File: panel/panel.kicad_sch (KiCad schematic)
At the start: 32 parts

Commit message: Moving panel to subfolder
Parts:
- J? (x2): footprint ledcube:5034800600 -> panel:5034800600
- U? (x2): symbol ledcube:SN74HC595 -> panel:SN74HC595
- U? (x3): symbol ledcube:TLC59025 -> panel:TLC59025
- U? (x2): symbol ledcube:NC7WZ17 -> panel:NC7WZ17

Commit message: Annotated schematic
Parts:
- gave numbers to parts that had none: 32

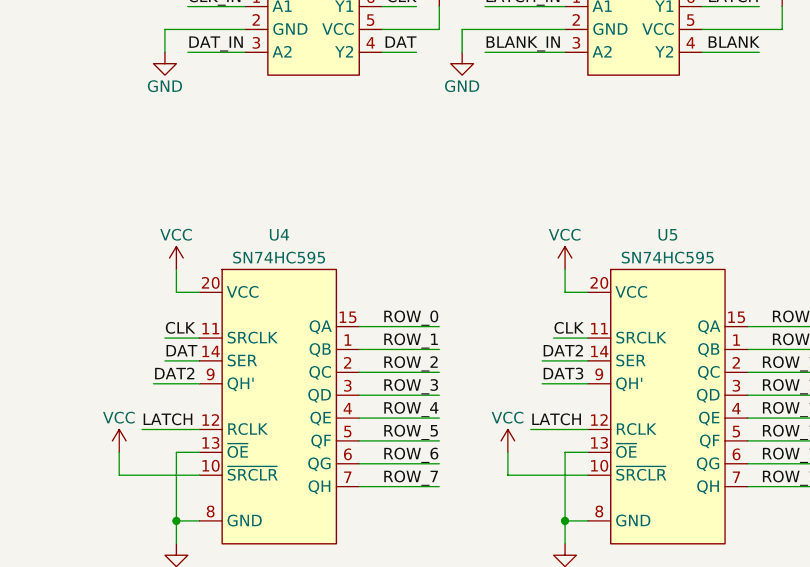
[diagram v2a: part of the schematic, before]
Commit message: LED matrix placement
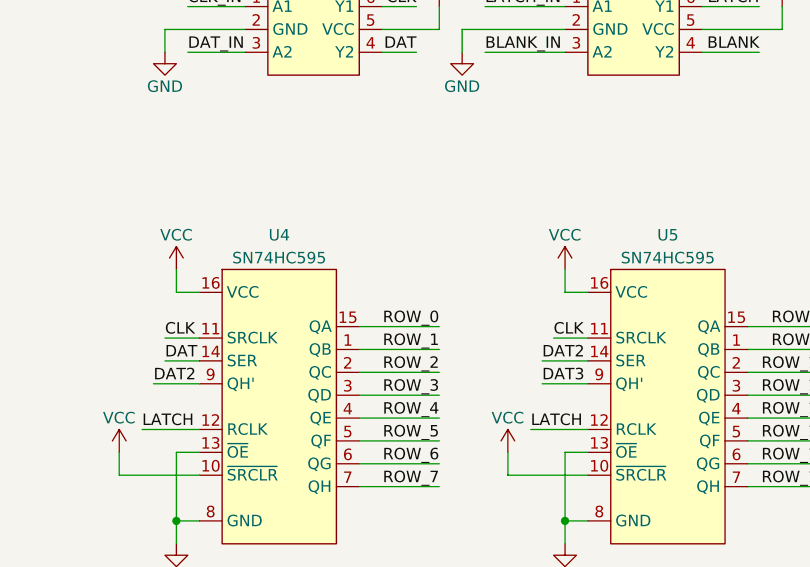
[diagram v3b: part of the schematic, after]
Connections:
- net VCC: now also U4.16 (VCC), U5.16 (VCC); no longer U4.20 (VCC), U5.20 (VCC)
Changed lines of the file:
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@@
     (pin "14")
     (pin "15")
+    (pin "16")
     (pin "2")
-    (pin "20")
     (pin "3")
     (pin "4")
@@
     (pin "14")
     (pin "15")
+    (pin "16")
     (pin "2")
-    (pin "20")
     (pin "3")
     (pin "4")
@@
     (pin "9")
   )
-  (symbol (lib_id "panel:TLC59025") (at 46.99 142.24 0) (unit 1)
+  (symbol (lib_name "panel:TLC59025_1") (lib_id "panel:TLC59025") (at 46.99 142.24 0) (unit 1)
     (in_bom yes) (on_board yes) (fields_autoplaced)
     (property "Reference" "U1" (id 0) (at 46.99 138.43 0))
@@
     (pin "9")
   )
-  (symbol (lib_id "panel:TLC59025") (at 90.17 142.24 0) (unit 1)
+  (symbol (lib_name "panel:TLC59025_2") (lib_id "panel:TLC59025") (at 90.17 142.24 0) (unit 1)
     (in_bom yes) (on_board yes) (fields_autoplaced)
     (property "Reference" "U2" (id 0) (at 90.17 138.43 0))

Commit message: Routed all data signals
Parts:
- Q1, Q10, Q11, Q12, Q13, Q14, Q15, Q16, Q2, Q3, Q4, Q5, Q6, Q7, Q8, Q9: footprint Package_TO_SOT_SMD:SOT-883 -> panel:SOT-883
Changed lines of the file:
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@@
       (effects (font (size 1.27 1.27)) (justify left) hide)
     )
-    (property "Footprint" "Package_TO_SOT_SMD:SOT-883" (id 2) (at 203.2 48.26 0)
+    (property "Footprint" "panel:SOT-883" (id 2) (at 203.2 48.26 0)
       (effects (font (size 1.27 1.27)) hide)
     )
@@
       (effects (font (size 1.27 1.27)) (justify left) hide)
     )
-    (property "Footprint" "Package_TO_SOT_SMD:SOT-883" (id 2) (at 203.2 59.69 0)
+    (property "Footprint" "panel:SOT-883" (id 2) (at 203.2 59.69 0)
       (effects (font (size 1.27 1.27)) hide)
     )
@@
       (effects (font (size 1.27 1.27)) (justify left) hide)
     )
-    (property "Footprint" "Package_TO_SOT_SMD:SOT-883" (id 2) (at 203.2 71.12 0)
+    (property "Footprint" "panel:SOT-883" (id 2) (at 203.2 71.12 0)
       (effects (font (size 1.27 1.27)) hide)
     )
@@
       (effects (font (size 1.27 1.27)) (justify left) hide)
     )
-    (property "Footprint" "Package_TO_SOT_SMD:SOT-883" (id 2) (at 203.2 82.55 0)
+    (property "Footprint" "panel:SOT-883" (id 2) (at 203.2 82.55 0)
       (effects (font (size 1.27 1.27)) hide)
     )
@@
       (effects (font (size 1.27 1.27)) (justify left) hide)
     )
-    (property "Footprint" "Package_TO_SOT_SMD:SOT-883" (id 2) (at 203.2 93.98 0)
+    (property "Footprint" "panel:SOT-883" (id 2) (at 203.2 93.98 0)
       (effects (font (size 1.27 1.27)) hide)
     )
@@
       (effects (font (size 1.27 1.27)) (justify left) hide)
     )
-    (property "Footprint" "Package_TO_SOT_SMD:SOT-883" (id 2) (at 203.2 105.41 0)
+    (property "Footprint" "panel:SOT-883" (id 2) (at 203.2 105.41 0)
       (effects (font (size 1.27 1.27)) hide)
     )
@@
       (effects (font (size 1.27 1.27)) (justify left) hide)
     )
-    (property "Footprint" "Package_TO_SOT_SMD:SOT-883" (id 2) (at 203.2 116.84 0)
+    (property "Footprint" "panel:SOT-883" (id 2) (at 203.2 116.84 0)
       (effects (font (size 1.27 1.27)) hide)
     )
@@
       (effects (font (size 1.27 1.27)) (justify left) hide)
     )
-    (property "Footprint" "Package_TO_SOT_SMD:SOT-883" (id 2) (at 203.2 128.27 0)
+    (property "Footprint" "panel:SOT-883" (id 2) (at 203.2 128.27 0)
       (effects (font (size 1.27 1.27)) hide)
     )
@@
       (effects (font (size 1.27 1.27)) (justify left) hide)
     )
-    (property "Footprint" "Package_TO_SOT_SMD:SOT-883" (id 2) (at 250.19 48.26 0)
+    (property "Footprint" "panel:SOT-883" (id 2) (at 250.19 48.26 0)
       (effects (font (size 1.27 1.27)) hide)
     )
@@
       (effects (font (size 1.27 1.27)) (justify left) hide)
     )
-    (property "Footprint" "Package_TO_SOT_SMD:SOT-883" (id 2) (at 250.19 59.69 0)
+    (property "Footprint" "panel:SOT-883" (id 2) (at 250.19 59.69 0)
       (effects (font (size 1.27 1.27)) hide)
     )
@@
       (effects (font (size 1.27 1.27)) (justify left) hide)
     )
-    (property "Footprint" "Package_TO_SOT_SMD:SOT-883" (id 2) (at 250.19 71.12 0)
+    (property "Footprint" "panel:SOT-883" (id 2) (at 250.19 71.12 0)
       (effects (font (size 1.27 1.27)) hide)
     )
@@
       (effects (font (size 1.27 1.27)) (justify left) hide)
     )
-    (property "Footprint" "Package_TO_SOT_SMD:SOT-883" (id 2) (at 250.19 82.55 0)
+    (property "Footprint" "panel:SOT-883" (id 2) (at 250.19 82.55 0)
       (effects (font (size 1.27 1.27)) hide)
     )
@@
       (effects (font (size 1.27 1.27)) (justify left) hide)
     )
-    (property "Footprint" "Package_TO_SOT_SMD:SOT-883" (id 2) (at 250.19 93.98 0)
+    (property "Footprint" "panel:SOT-883" (id 2) (at 250.19 93.98 0)
       (effects (font (size 1.27 1.27)) hide)
     )
@@
       (effects (font (size 1.27 1.27)) (justify left) hide)
     )
-    (property "Footprint" "Package_TO_SOT_SMD:SOT-883" (id 2) (at 250.19 105.41 0)
+    (property "Footprint" "panel:SOT-883" (id 2) (at 250.19 105.41 0)
       (effects (font (size 1.27 1.27)) hide)
     )
@@
       (effects (font (size 1.27 1.27)) (justify left) hide)
     )
-    (property "Footprint" "Package_TO_SOT_SMD:SOT-883" (id 2) (at 250.19 116.84 0)
+    (property "Footprint" "panel:SOT-883" (id 2) (at 250.19 116.84 0)
       (effects (font (size 1.27 1.27)) hide)
     )
@@
       (effects (font (size 1.27 1.27)) (justify left) hide)
     )
-    (property "Footprint" "Package_TO_SOT_SMD:SOT-883" (id 2) (at 250.19 128.27 0)
+    (property "Footprint" "panel:SOT-883" (id 2) (at 250.19 128.27 0)
       (effects (font (size 1.27 1.27)) hide)
     )
@@
     )
     (path "/540dc0a0-cb0b-4dfb-87f6-511342a2796f"
-      (reference "Q1") (unit 1) (value "Q_PMOS_GSD") (footprint "Package_TO_SOT_SMD:SOT-883")
+      (reference "Q1") (unit 1) (value "Q_PMOS_GSD") (footprint "panel:SOT-883")
     )
     (path "/6df639de-66aa-4f8e-934a-38515961a4c1"
-      (reference "Q2") (unit 1) (value "Q_PMOS_GSD") (footprint "Package_TO_SOT_SMD:SOT-883")
+      (reference "Q2") (unit 1) (value "Q_PMOS_GSD") (footprint "panel:SOT-883")
     )
     (path "/1662c1e9-d071-4672-a50a-d59632799096"
-      (reference "Q3") (unit 1) (value "Q_PMOS_GSD") (footprint "Package_TO_SOT_SMD:SOT-883")
+      (reference "Q3") (unit 1) (value "Q_PMOS_GSD") (footprint "panel:SOT-883")
     )
     (path "/e62bc1a4-9007-492e-9214-cdaf7f9883a8"
-      (reference "Q4") (unit 1) (value "Q_PMOS_GSD") (footprint "Package_TO_SOT_SMD:SOT-883")
+      (reference "Q4") (unit 1) (value "Q_PMOS_GSD") (footprint "panel:SOT-883")
     )
     (path "/b0fe76a1-e7b8-4c55-ba03-bdfd4116e876"
-      (reference "Q5") (unit 1) (value "Q_PMOS_GSD") (footprint "Package_TO_SOT_SMD:SOT-883")
+      (reference "Q5") (unit 1) (value "Q_PMOS_GSD") (footprint "panel:SOT-883")
     )
     (path "/f9b833db-6f56-4fac-a5e4-cddc32cf4c6b"
-      (reference "Q6") (unit 1) (value "Q_PMOS_GSD") (footprint "Package_TO_SOT_SMD:SOT-883")
+      (reference "Q6") (unit 1) (value "Q_PMOS_GSD") (footprint "panel:SOT-883")
     )
     (path "/1979edeb-c786-4256-9b38-790a807c310d"
-      (reference "Q7") (unit 1) (value "Q_PMOS_GSD") (footprint "Package_TO_SOT_SMD:SOT-883")
+      (reference "Q7") (unit 1) (value "Q_PMOS_GSD") (footprint "panel:SOT-883")
     )
     (path "/7d404bbb-94fd-4b28-9150-5e5942e1a641"
-      (reference "Q8") (unit 1) (value "Q_PMOS_GSD") (footprint "Package_TO_SOT_SMD:SOT-883")
+      (reference "Q8") (unit 1) (value "Q_PMOS_GSD") (footprint "panel:SOT-883")
     )
     (path "/6f3a29fc-6cb3-44c9-948c-d864912cc61c"
-      (reference "Q9") (unit 1) (value "Q_PMOS_GSD") (footprint "Package_TO_SOT_SMD:SOT-883")
+      (reference "Q9") (unit 1) (value "Q_PMOS_GSD") (footprint "panel:SOT-883")
     )
     (path "/d31cec0c-c84b-4cf9-a596-e42b38fcb696"
-      (reference "Q10") (unit 1) (value "Q_PMOS_GSD") (footprint "Package_TO_SOT_SMD:SOT-883")
+      (reference "Q10") (unit 1) (value "Q_PMOS_GSD") (footprint "panel:SOT-883")
     )
     (path "/0a43e7b4-017b-4935-978c-84fb9a5a6cc0"
-      (reference "Q11") (unit 1) (value "Q_PMOS_GSD") (footprint "Package_TO_SOT_SMD:SOT-883")
+      (reference "Q11") (unit 1) (value "Q_PMOS_GSD") (footprint "panel:SOT-883")
     )
     (path "/5e86269f-d809-4ae3-ae14-44b60a3b5dec"
-      (reference "Q12") (unit 1) (value "Q_PMOS_GSD") (footprint "Package_TO_SOT_SMD:SOT-883")
+      (reference "Q12") (unit 1) (value "Q_PMOS_GSD") (footprint "panel:SOT-883")
     )
     (path "/1fdad119-9c7a-4284-83e9-942858cd8950"
-      (reference "Q13") (unit 1) (value "Q_PMOS_GSD") (footprint "Package_TO_SOT_SMD:SOT-883")
+      (reference "Q13") (unit 1) (value "Q_PMOS_GSD") (footprint "panel:SOT-883")
     )
     (path "/b6fd7422-90bb-4e64-886e-0887f176a800"
-      (reference "Q14") (unit 1) (value "Q_PMOS_GSD") (footprint "Package_TO_SOT_SMD:SOT-883")
+      (reference "Q14") (unit 1) (value "Q_PMOS_GSD") (footprint "panel:SOT-883")
     )
     (path "/77755fd0-ff8f-4a33-bd6a-dc738f7f8057"
-      (reference "Q15") (unit 1) (value "Q_PMOS_GSD") (footprint "Package_TO_SOT_SMD:SOT-883")
+      (reference "Q15") (unit 1) (value "Q_PMOS_GSD") (footprint "panel:SOT-883")
     )
     (path "/d1db849d-984c-4d78-a6a1-13bc0eace430"
-      (reference "Q16") (unit 1) (value "Q_PMOS_GSD") (footprint "Package_TO_SOT_SMD:SOT-883")
+      (reference "Q16") (unit 1) (value "Q_PMOS_GSD") (footprint "panel:SOT-883")
     )
     (path "/52b80c72-d096-46bf-b96a-1dc1d5e2cd56"

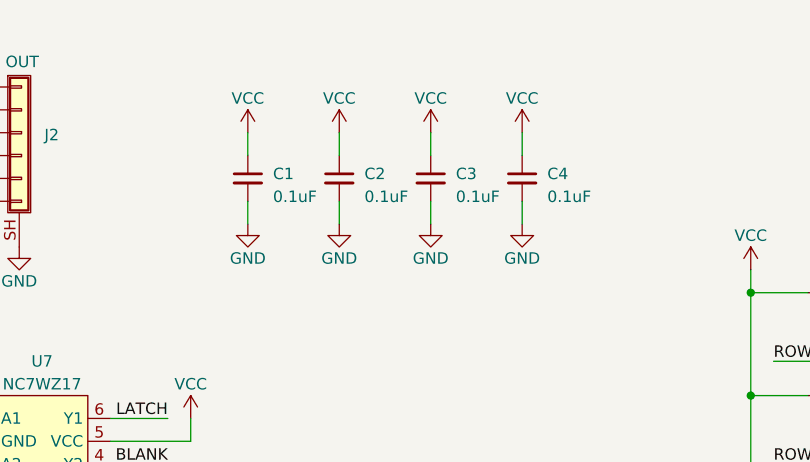
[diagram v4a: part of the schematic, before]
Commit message: Placed decoupling caps
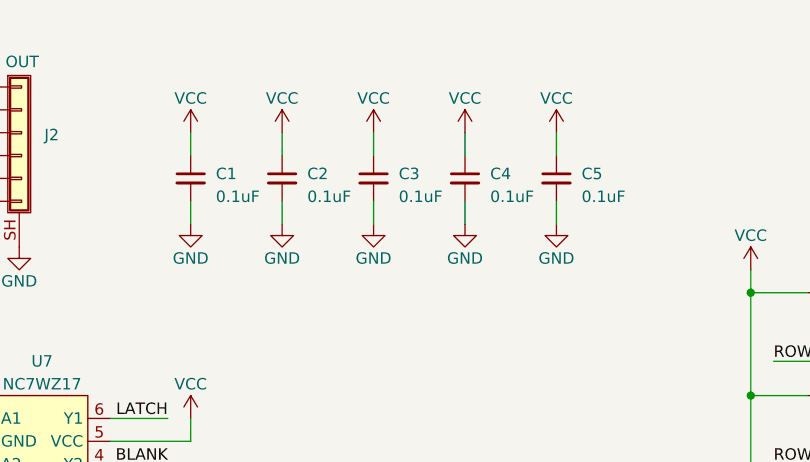
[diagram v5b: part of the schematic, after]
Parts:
- added C5: 0.1uF, Capacitor_SMD:C_0402_1005Metric, symbol Device:C_Small
- C1, C2, C3, C4: footprint Capacitor_SMD:C_0603_1608Metric -> Capacitor_SMD:C_0402_1005Metric
- R1, R2, R3: footprint Resistor_SMD:R_0603_1608Metric -> Resistor_SMD:R_0402_1005Metric
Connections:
- net GND: now also C5.2
- net VCC: now also C5.1
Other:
- moved on the sheet: C1, C2, C3, C4

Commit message: Silkscreen cleanup
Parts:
- C1, C2, C3, C4, C5: footprint Capacitor_SMD:C_0402_1005Metric -> panel:C_0402_1005Metric
- R1, R2, R3: footprint Resistor_SMD:R_0402_1005Metric -> panel:R_0402_1005Metric
- U1, U2, U3: footprint Package_SO:SSOP-24_3.9x8.7mm_P0.635mm -> panel:SSOP-24_3.9x8.7mm_P0.635mm
- U4, U5: footprint Package_SO:TSSOP-16_4.4x5mm_P0.65mm -> panel:TSSOP-16_4.4x5mm_P0.65mm
- U6, U7: footprint Package_SON:Fairchild_MicroPak2-6_1.0x1.0mm_P0.35mm -> panel:Fairchild_MicroPak2-6_1.0x1.0mm_P0.35mm
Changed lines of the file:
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@@
       (effects (font (size 1.27 1.27)) (justify right))
     )
-    (property "Footprint" "Resistor_SMD:R_0402_1005Metric" (id 2) (at 35.56 175.26 0)
+    (property "Footprint" "panel:R_0402_1005Metric" (id 2) (at 35.56 175.26 0)
       (effects (font (size 1.27 1.27)) hide)
     )
@@
       (effects (font (size 1.27 1.27)) (justify right))
     )
-    (property "Footprint" "Resistor_SMD:R_0402_1005Metric" (id 2) (at 78.74 175.26 0)
+    (property "Footprint" "panel:R_0402_1005Metric" (id 2) (at 78.74 175.26 0)
       (effects (font (size 1.27 1.27)) hide)
     )
@@
       (effects (font (size 1.27 1.27)) (justify right))
     )
-    (property "Footprint" "Resistor_SMD:R_0402_1005Metric" (id 2) (at 121.92 175.26 0)
+    (property "Footprint" "panel:R_0402_1005Metric" (id 2) (at 121.92 175.26 0)
       (effects (font (size 1.27 1.27)) hide)
     )
@@
       (effects (font (size 1.27 1.27)) (justify left))
     )
-    (property "Footprint" "Capacitor_SMD:C_0402_1005Metric" (id 2) (at 127 38.1 0)
+    (property "Footprint" "panel:C_0402_1005Metric" (id 2) (at 127 38.1 0)
       (effects (font (size 1.27 1.27)) hide)
     )
@@
       (effects (font (size 1.27 1.27)) (justify left))
     )
-    (property "Footprint" "Capacitor_SMD:C_0402_1005Metric" (id 2) (at 137.16 38.1 0)
+    (property "Footprint" "panel:C_0402_1005Metric" (id 2) (at 137.16 38.1 0)
       (effects (font (size 1.27 1.27)) hide)
     )
@@
       (effects (font (size 1.27 1.27)) (justify left))
     )
-    (property "Footprint" "Capacitor_SMD:C_0402_1005Metric" (id 2) (at 147.32 38.1 0)
+    (property "Footprint" "panel:C_0402_1005Metric" (id 2) (at 147.32 38.1 0)
       (effects (font (size 1.27 1.27)) hide)
     )
@@
       (effects (font (size 1.27 1.27)) (justify left))
     )
-    (property "Footprint" "Capacitor_SMD:C_0402_1005Metric" (id 2) (at 157.48 38.1 0)
+    (property "Footprint" "panel:C_0402_1005Metric" (id 2) (at 157.48 38.1 0)
       (effects (font (size 1.27 1.27)) hide)
     )
@@
       (effects (font (size 1.27 1.27)) (justify left))
     )
-    (property "Footprint" "Capacitor_SMD:C_0402_1005Metric" (id 2) (at 167.64 38.1 0)
+    (property "Footprint" "panel:C_0402_1005Metric" (id 2) (at 167.64 38.1 0)
       (effects (font (size 1.27 1.27)) hide)
     )
@@
     (property "Reference" "U6" (id 0) (at 74.93 58.42 0))
     (property "Value" "NC7WZ17" (id 1) (at 74.93 60.96 0))
-    (property "Footprint" "Package_SON:Fairchild_MicroPak2-6_1.0x1.0mm_P0.35mm" (id 2) (at 74.93 76.2 0)
+    (property "Footprint" "panel:Fairchild_MicroPak2-6_1.0x1.0mm_P0.35mm" (id 2) (at 74.93 76.2 0)
       (effects (font (size 1.27 1.27)) hide)
     )
@@
     (property "Reference" "U7" (id 0) (at 110.49 58.42 0))
     (property "Value" "NC7WZ17" (id 1) (at 110.49 60.96 0))
-    (property "Footprint" "Package_SON:Fairchild_MicroPak2-6_1.0x1.0mm_P0.35mm" (id 2) (at 110.49 76.2 0)
+    (property "Footprint" "panel:Fairchild_MicroPak2-6_1.0x1.0mm_P0.35mm" (id 2) (at 110.49 76.2 0)
       (effects (font (size 1.27 1.27)) hide)
     )
@@
     (property "Reference" "U4" (id 0) (at 71.12 90.17 0))
     (property "Value" "SN74HC595" (id 1) (at 71.12 92.71 0))
-    (property "Footprint" "Package_SO:TSSOP-16_4.4x5mm_P0.65mm" (id 2) (at 71.12 128.27 0)
+    (property "Footprint" "panel:TSSOP-16_4.4x5mm_P0.65mm" (id 2) (at 71.12 128.27 0)
       (effects (font (size 1.27 1.27)) hide)
     )
@@
     (property "Reference" "U5" (id 0) (at 114.3 90.17 0))
     (property "Value" "SN74HC595" (id 1) (at 114.3 92.71 0))
-    (property "Footprint" "Package_SO:TSSOP-16_4.4x5mm_P0.65mm" (id 2) (at 114.3 128.27 0)
+    (property "Footprint" "panel:TSSOP-16_4.4x5mm_P0.65mm" (id 2) (at 114.3 128.27 0)
       (effects (font (size 1.27 1.27)) hide)
     )
@@
     (property "Reference" "U1" (id 0) (at 46.99 138.43 0))
     (property "Value" "TLC59025" (id 1) (at 46.99 140.97 0))
-    (property "Footprint" "Package_SO:SSOP-24_3.9x8.7mm_P0.635mm" (id 2) (at 46.99 189.23 0)
+    (property "Footprint" "panel:SSOP-24_3.9x8.7mm_P0.635mm" (id 2) (at 46.99 189.23 0)
       (effects (font (size 1.27 1.27)) hide)
     )
@@
     (property "Reference" "U2" (id 0) (at 90.17 138.43 0))
     (property "Value" "TLC59025" (id 1) (at 90.17 140.97 0))
-    (property "Footprint" "Package_SO:SSOP-24_3.9x8.7mm_P0.635mm" (id 2) (at 90.17 189.23 0)
+    (property "Footprint" "panel:SSOP-24_3.9x8.7mm_P0.635mm" (id 2) (at 90.17 189.23 0)
       (effects (font (size 1.27 1.27)) hide)
     )
@@
     (property "Reference" "U3" (id 0) (at 133.35 138.43 0))
     (property "Value" "TLC59025" (id 1) (at 133.35 140.97 0))
-    (property "Footprint" "Package_SO:SSOP-24_3.9x8.7mm_P0.635mm" (id 2) (at 133.35 189.23 0)
+    (property "Footprint" "panel:SSOP-24_3.9x8.7mm_P0.635mm" (id 2) (at 133.35 189.23 0)
       (effects (font (size 1.27 1.27)) hide)
     )
@@
     )
     (path "/0e22ebf2-10c4-4bf3-ac1b-f1cc2a956539"
-      (reference "C1") (unit 1) (value "0.1uF") (footprint "Capacitor_SMD:C_0402_1005Metric")
+      (reference "C1") (unit 1) (value "0.1uF") (footprint "panel:C_0402_1005Metric")
     )
     (path "/a534d243-1440-4835-8d42-537a3e782116"
-      (reference "C2") (unit 1) (value "0.1uF") (footprint "Capacitor_SMD:C_0402_1005Metric")
+      (reference "C2") (unit 1) (value "0.1uF") (footprint "panel:C_0402_1005Metric")
     )
     (path "/5405845a-6c34-40fc-8dda-a6e36dc2ea71"
-      (reference "C3") (unit 1) (value "0.1uF") (footprint "Capacitor_SMD:C_0402_1005Metric")
+      (reference "C3") (unit 1) (value "0.1uF") (footprint "panel:C_0402_1005Metric")
     )
     (path "/b5504b42-8c3f-4c96-92cd-452421bb032d"
-      (reference "C4") (unit 1) (value "0.1uF") (footprint "Capacitor_SMD:C_0402_1005Metric")
+      (reference "C4") (unit 1) (value "0.1uF") (footprint "panel:C_0402_1005Metric")
     )
     (path "/c79132e1-defe-4208-9a46-bf75965e34df"
-      (reference "C5") (unit 1) (value "0.1uF") (footprint "Capacitor_SMD:C_0402_1005Metric")
+      (reference "C5") (unit 1) (value "0.1uF") (footprint "panel:C_0402_1005Metric")
     )
     (path "/7a0eb2e8-7ef5-4ea7-9902-0f9a9ccf40f3/169b3fa0-f652-4440-8dd7-598c74a2653c"
@@
     )
     (path "/52b80c72-d096-46bf-b96a-1dc1d5e2cd56"
-      (reference "R1") (unit 1) (value "2.2k") (footprint "Resistor_SMD:R_0402_1005Metric")
+      (reference "R1") (unit 1) (value "2.2k") (footprint "panel:R_0402_1005Metric")
     )
     (path "/1ae57071-a5b8-464f-828c-0e455783e6a4"
-      (reference "R2") (unit 1) (value "7.5k") (footprint "Resistor_SMD:R_0402_1005Metric")
+      (reference "R2") (unit 1) (value "7.5k") (footprint "panel:R_0402_1005Metric")
     )
     (path "/cb05707f-f511-43ce-8d99-48fab753d2a1"
-      (reference "R3") (unit 1) (value "4.12k") (footprint "Resistor_SMD:R_0402_1005Metric")
+      (reference "R3") (unit 1) (value "4.12k") (footprint "panel:R_0402_1005Metric")
     )
     (path "/b4b71254-1f6d-4f29-8e83-69885988906a"
-      (reference "U1") (unit 1) (value "TLC59025") (footprint "Package_SO:SSOP-24_3.9x8.7mm_P0.635mm")
+      (reference "U1") (unit 1) (value "TLC59025") (footprint "panel:SSOP-24_3.9x8.7mm_P0.635mm")
     )
     (path "/469f4872-4890-4394-bf3c-b177ce73e86d"
-      (reference "U2") (unit 1) (value "TLC59025") (footprint "Package_SO:SSOP-24_3.9x8.7mm_P0.635mm")
+      (reference "U2") (unit 1) (value "TLC59025") (footprint "panel:SSOP-24_3.9x8.7mm_P0.635mm")
     )
     (path "/83ad91c3-617f-47ac-a474-8298d9b7438e"
-      (reference "U3") (unit 1) (value "TLC59025") (footprint "Package_SO:SSOP-24_3.9x8.7mm_P0.635mm")
+      (reference "U3") (unit 1) (value "TLC59025") (footprint "panel:SSOP-24_3.9x8.7mm_P0.635mm")
     )
     (path "/0e9dbd11-fcbb-4bd2-9edb-9b32f0625e17"
-      (reference "U4") (unit 1) (value "SN74HC595") (footprint "Package_SO:TSSOP-16_4.4x5mm_P0.65mm")
+      (reference "U4") (unit 1) (value "SN74HC595") (footprint "panel:TSSOP-16_4.4x5mm_P0.65mm")
     )
     (path "/5c0b5abc-d0d8-494a-9785-96032406e3ec"
-      (reference "U5") (unit 1) (value "SN74HC595") (footprint "Package_SO:TSSOP-16_4.4x5mm_P0.65mm")
+      (reference "U5") (unit 1) (value "SN74HC595") (footprint "panel:TSSOP-16_4.4x5mm_P0.65mm")
     )
     (path "/df80874c-250f-4784-aef1-7810512a1578"
-      (reference "U6") (unit 1) (value "NC7WZ17") (footprint "Package_SON:Fairchild_MicroPak2-6_1.0x1.0mm_P0.35mm")
+      (reference "U6") (unit 1) (value "NC7WZ17") (footprint "panel:Fairchild_MicroPak2-6_1.0x1.0mm_P0.35mm")
     )
     (path "/9d75a2f3-9d0d-4c0b-b26a-abbf8cbe83d5"
-      (reference "U7") (unit 1) (value "NC7WZ17") (footprint "Package_SON:Fairchild_MicroPak2-6_1.0x1.0mm_P0.35mm")
-    )
-  )
+      (reference "U7") (unit 1) (value "NC7WZ17") (footprint "panel:Fairchild_MicroPak2-6_1.0x1.0mm_P0.35mm")
+    )
+  )
